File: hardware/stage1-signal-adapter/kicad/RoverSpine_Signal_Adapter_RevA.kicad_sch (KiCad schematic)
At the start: 2 parts, among them J1 RPI_GPIO_2x20, J2 D50A_CONTROL_2x5

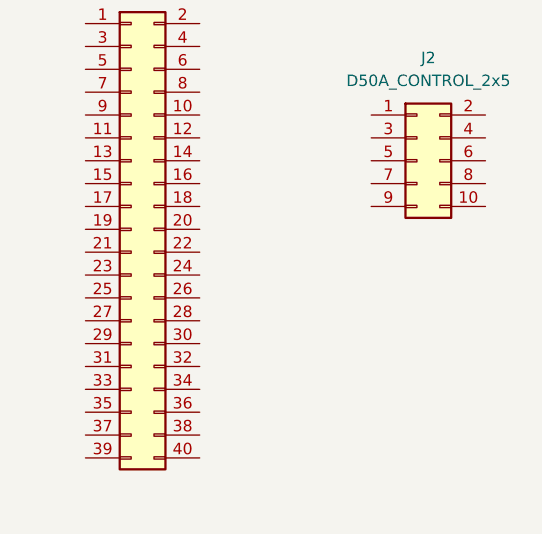
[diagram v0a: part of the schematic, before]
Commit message: Correct the D50A control header: V must be connected, and it is ten wires
Two factual errors in this repository's own records, found from the RoverPi
wiring table and photographs of the board. One of them would have produced a
dead board. Written up in
docs/devlog/2026-09-12-d50a-control-header-correction.md.

V is not the driver offering power outward. It is the 3.3 V rail that powers
the input side of the driver's galvanic isolation, and Rev A was specified to
leave both V pins unconnected. That board would have soldered up, plugged in,
and moved nothing at all - with no control signal working and no obvious
reason why.

The wrong belief traces to the 2026-09-11 signal map, which recorded seven
connections and omitted both V pins and the second G. The decision was then
made consistently with an incomplete map. The lesson is not "check harder":
that map had no citation, and the corrected one names the RoverPi wiring table
as its source.

So Rev A is ten copper connections forming eight nets, not seven of each.

The correction also produces a stronger argument for the board than the README
was making. On the Pi header 3.3 V is pins 1 and 17 while 5 V is pins 2 and 4,
one row over and immediately adjacent, and 5 V into a 3.3 V isolated input is
a damaged part rather than a stall. A dupont wire can be moved there in a
second; a copper trace cannot be mis-plugged at all. That failure mode
disappears permanently, which is worth more than the vibration argument.

Also confirmed from the photographs, and also a correction: the D50A's control
header is a shrouded boxed header, so that end is keyed by the manufacturer.
An earlier claim the same day - that keying would only protect the adapter's
own end - is withdrawn. A matching DC3-10P at J2 makes both ends keyed, so it
is now a requirement rather than a preference. The Pi's 40-pin header is still
unshrouded and still relies on the red stripe.

Two things are deliberately left unresolved rather than guessed:

- Which physi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
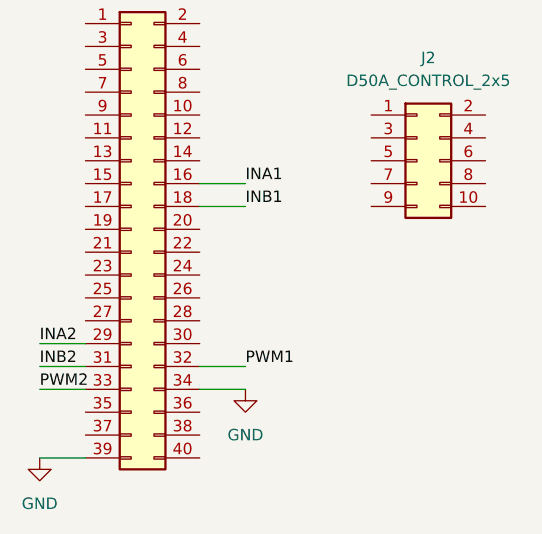
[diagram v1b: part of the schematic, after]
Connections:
- net INA1: now reaches J1.16 (Pin_16)
- net INB1: now reaches J1.18 (Pin_18)
- net INA2: now reaches J1.29 (Pin_29)
- net INB2: now reaches J1.31 (Pin_31)
- net PWM1: now reaches J1.32 (Pin_32)
- net PWM2: now reaches J1.33 (Pin_33)
- net GND: now reaches J1.34 (Pin_34)
- net GND: now also J1.39 (Pin_39)

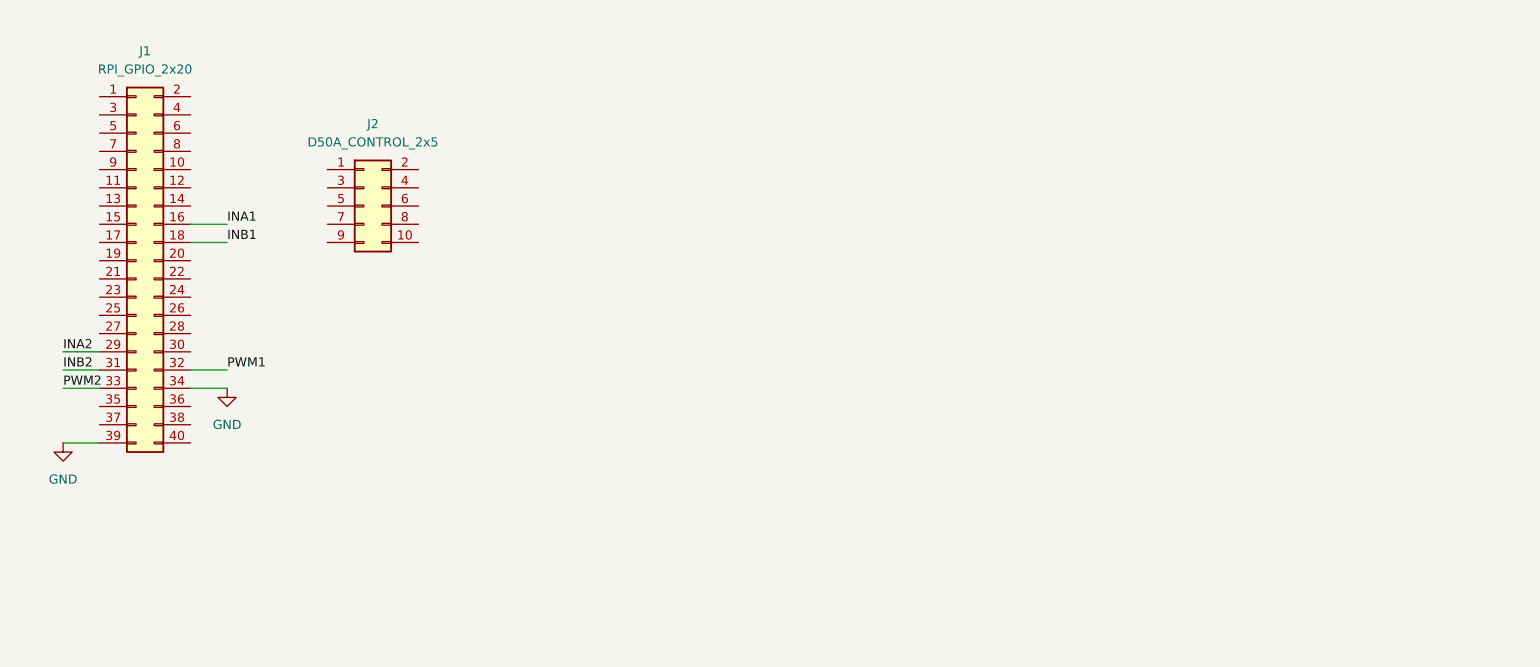
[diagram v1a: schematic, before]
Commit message: Finish the Rev A schematic, and verify it against the signal map
Ten connections forming eight nets, drawn with net labels on stubs rather
than wires across the sheet, with GND and +3V3 as power symbols and one
PWR_FLAG per rail. ERC sits at 30 errors and 0 warnings, and both numbers
reconcile exactly: 30 is J1's forty pins minus the ten used, and zero
warnings means all six signal nets now have two pins each. Not one
violation is unaccounted for. Written up in
docs/devlog/2026-09-12-revA-schematic-complete.md.

ERC passing is not the same as the board being right, and that is the
lesson worth keeping from today. Had PWM1 and PWM2 been swapped onto each
other's J2 pins, both nets would still connect exactly two pins and ERC
would still report 30/0 - and the board would ship with the left and
right motors' speed control reversed. ERC checks structure, not intent;
it has no idea GPIO12 was supposed to reach P1. So the netlist was
exported and every net's membership compared to the signal map as
strings. All eight pass, thirty single-pin unconnected nets as expected,
no extra nets. The netlist itself is not committed - it is generated,
reproducible, and gitignored; what is committed is its source and this
record of the comparison.

One ERC error along the way was worth having. The count read 43 where 42
was expected, and the extra one was a power input not driven by any power
output. ERC was right: there is genuinely no power source on this
schematic, since 3.3 V and ground arrive from the Pi over a ribbon. The
fix is a PWR_FLAG, which declares that the rail is supplied from outside
the sheet - true here, which is what makes it legitimate rather than a
way to silence a complaint. Recorded because Stage 4 has a real
regulator, and the same error there would be a real fault. PWR_FLAG is a
declaration, never a mute button.

One assumption remains: J2's numbering rests on "square pad = pin 1", a
common PCB convention rather than a standard. What is measured is that
the squ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
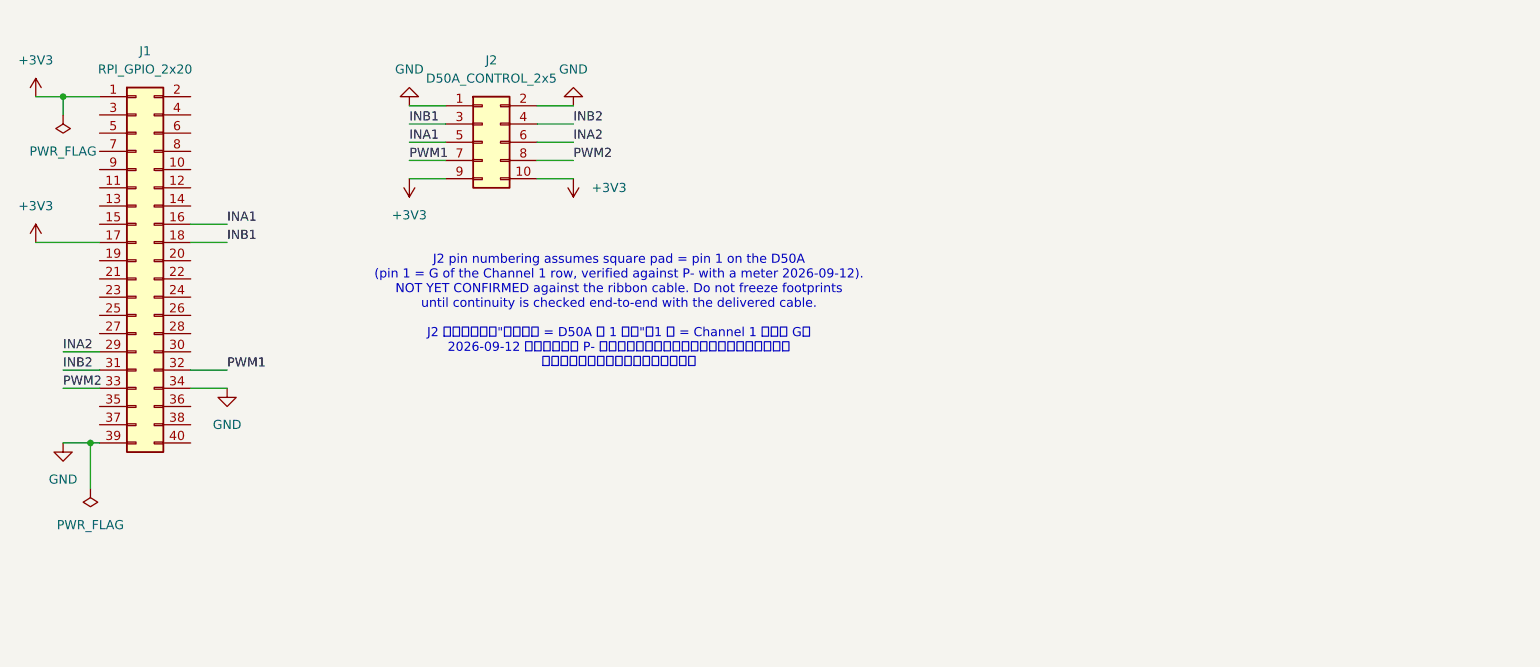
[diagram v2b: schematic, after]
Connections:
- net GND: now also J2.1 (Pin_1), J2.2 (Pin_2)
- net INA1: now also J2.5 (Pin_5)
- net INA2: now also J2.6 (Pin_6)
- net INB1: now also J2.3 (Pin_3)
- net INB2: now also J2.4 (Pin_4)
- net PWM1: now also J2.7 (Pin_7)
- net PWM2: now also J2.8 (Pin_8)
- net +3V3: now reaches J1.1 (Pin_1)
- net +3V3: now also J1.17 (Pin_17), J2.10 (Pin_10), J2.9 (Pin_9)
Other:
- note added: "J2 pin numbering assumes square pad = pin 1 on the D50A (pin 1 = G of the Channel 1 row, verified against P- with a meter 2026-09-12). NOT YET CONFIRMED against the ribbon cable. Do not freeze footprints until continuity is checked end-to-end with the delivered cable. J2 引脚编号基于"方形焊盘 = D50A 的 1 号脚"（1 号 = Channel 1 那排的 G， 2026-09-12 已用万用表对 P- 验证）。排线尚未到货，未做端到端实测确认。 锁定封装前必须用实物排线逐根量通。"
- moved on the sheet: J2

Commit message: Draw R1-R12: Rev A's schematic is complete at fourteen nets
Twelve resistors added as six identical blocks in empty sheet space, each one
PWM1 -> R series -> P1, with a pull-down from the driver side to GND. The
resistors are not drawn between J1 and J2; same-named labels put them in the
middle of a net without a line crossing the sheet.

ERC 30 errors / 0 warnings. Netlist check ALL PASS: 14 nets, every member
present, 30 single-pin nets as expected, no unexpected or auto-named nets.

Three things worth keeping from the session:

- A mislabel appeared and ERC stayed silent about it. One block fed by INB2 had
  its driver-side label left as P1 after a copy, which put PWM1's signal and
  INB2's signal on one net and left B2 unpaired. Every pin had a wire, every
  wire had a label, nothing dangled: the report was 30 / 0 with the fault
  present. This is yesterday's argument about ERC checking structure rather than
  intent, one day later and concrete. Caught by eye during review rather than by
  the checker, which had not been run yet — recorded that way because the honest
  point is not that the tool saved us. It is that the tool does not get tired on
  the sixth block.

- Six ERC warnings turned out to be one mistake copied five times: a 50 mil
  dangling wire end in the first block. The root cause was not a slip but
  Preferences -> Schematic Editor -> Grid Options -> Grid Overrides, which
  pinned wires and connected items to 50 mils — half the 100 mil grid the
  symbol pins sit on. A Grid Override outranks the active grid, so changing the
  grid would not have helped. Both overrides are now 100 mils.

- Reference numbering was redone by hand. KiCad auto-annotated series resistors
  onto odd numbers and pull-downs onto even ones; the design says R1-R6 series
  and R7-R12 pull-down. Grouping by function keeps the assembly instruction as
  one sentence instead of a list of six numbers to check against — read while
  holding an iron over a board that will not lie fla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
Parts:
- added R1, R2, R3, R4, R5, R6: 33, symbol Device:R
- added R10, R11, R12, R7, R8, R9: 10k, Package_QFP:PQFP-160_28x28mm_P0.65mm, symbol Device:R
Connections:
- net GND: now also R10.2, R11.2, R12.2, R7.2, R8.2, R9.2
- net INA1: now also R2.1; no longer J2.5 (Pin_5)
- net INA2: now also R5.1; no longer J2.6 (Pin_6)
- net INB1: now also R3.1; no longer J2.3 (Pin_3)
- net INB2: now also R6.1; no longer J2.4 (Pin_4)
- net PWM1: now also R1.1; no longer J2.7 (Pin_7)
- net PWM2: now also R4.1; no longer J2.8 (Pin_8)
- new net A1: J2.5 (Pin_5), R2.2, R8.1
- new net A2: J2.6 (Pin_6), R11.1, R5.2
- new net B1: J2.3 (Pin_3), R3.2, R9.1
- new net B2: J2.4 (Pin_4), R12.1, R6.2
- new net P1: J2.7 (Pin_7), R1.2, R7.1
- new net P2: J2.8 (Pin_8), R10.1, R4.2

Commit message: A 160-pin QFP was sitting on six resistors, and the count was blind to it
R7-R12, the 10 kOhm pull-downs, carried
Package_QFP:PQFP-160_28x28mm_P0.65mm - a 28x28 mm, 160-pin quad flat
pack. Introduced by 949f91a, committed and pushed, and present for a day
while every document in the repository said "footprints not assigned".

It came in the way the six dangling wire ends did, from the same
copy-paste into the same six blocks. That commit's devlog caught the wire
ends and concluded copy-paste makes mistakes easy to recognise as
systematic. True, and it still missed the second defect in the same six
symbols - because the rule that would have reported it, footprint_filter,
was set to ignore that day. Switched on hours later, it reported all six
immediately. Nobody read them as six.

Clearing them does not change the ERC total: 44 with the QFPs, 44
without. 30 pin_not_connected + 8 empty + 6 wrong becomes 30 + 14 empty.
So the check is not the count, it is the composition, and tools/README.md
now groups by the offending value rather than by the rule name - the
grouping that produced "14 [footprint_filter]" hid the distinction
between eight to do and six that were wrong.

Yesterday's correction claimed all fourteen were empty. It was eight and
six; that sentence generalised from three lines of a forty-four line
report. Third time in four days that a cheap stand-in was substituted for
the population - a panel for a run, a claim about the enclosure for a
measurement, three lines for forty-four.

So footprints are now compared against a written-down map by
check_nets.py, using the netlist it already parses. ERC cannot do this
job: R1-R12 all declare the filter R_*, which R_0805_2012Metric and
R_Axial_DIN0207_... match equally, so swapping the series resistors with
the pull-downs passes ERC at a clean 30 / 0. The map was written before
the footprints are assigned, so it fails today and the failure prints the
to-do list.

The Stage 1 exit criterion is corrected accordingly: 3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
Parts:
- R10, R11, R12, R7, R8, R9: footprint Package_QFP:PQFP-160_28x28mm_P0.65mm -> (none)
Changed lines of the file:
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@@
 			)
 		)
-		(property "Footprint" "Package_QFP:PQFP-160_28x28mm_P0.65mm"
+		(property "Footprint" ""
 			(at 183.642 72.39 90)
 			(hide yes)
@@
 			)
 		)
-		(property "Footprint" "Package_QFP:PQFP-160_28x28mm_P0.65mm"
+		(property "Footprint" ""
 			(at 224.282 101.6 90)
 			(hide yes)
@@
 			)
 		)
-		(property "Footprint" "Package_QFP:PQFP-160_28x28mm_P0.65mm"
+		(property "Footprint" ""
 			(at 223.012 41.91 90)
 			(hide yes)
@@
 			)
 		)
-		(property "Footprint" "Package_QFP:PQFP-160_28x28mm_P0.65mm"
+		(property "Footprint" ""
 			(at 224.282 72.39 90)
 			(hide yes)
@@
 			)
 		)
-		(property "Footprint" "Package_QFP:PQFP-160_28x28mm_P0.65mm"
+		(property "Footprint" ""
 			(at 184.912 101.6 90)
 			(hide yes)
@@
 			)
 		)
-		(property "Footprint" "Package_QFP:PQFP-160_28x28mm_P0.65mm"
+		(property "Footprint" ""
 			(at 182.372 41.91 90)
 			(hide yes)
